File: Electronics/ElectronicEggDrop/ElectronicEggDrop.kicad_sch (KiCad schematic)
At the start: 10 parts, among them U1 LIS3DH

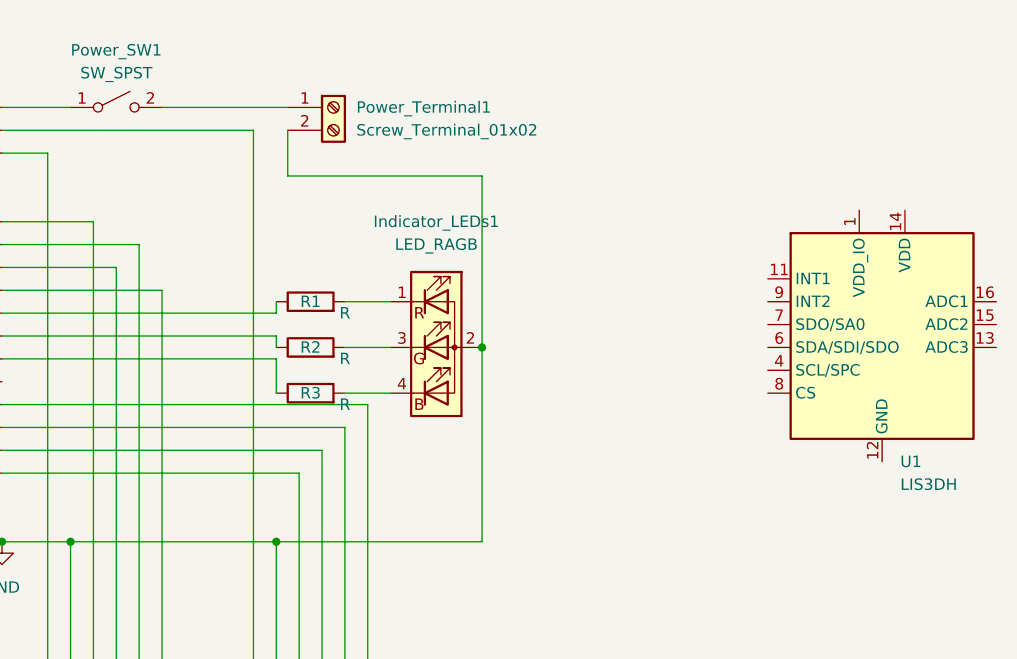
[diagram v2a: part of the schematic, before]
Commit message: Finished V1 of the Control and Sensor Egg boards, 3D models created by FreeCAD.  Need to fix code, assemble boards in FreeCAD, and create 3D printed housing
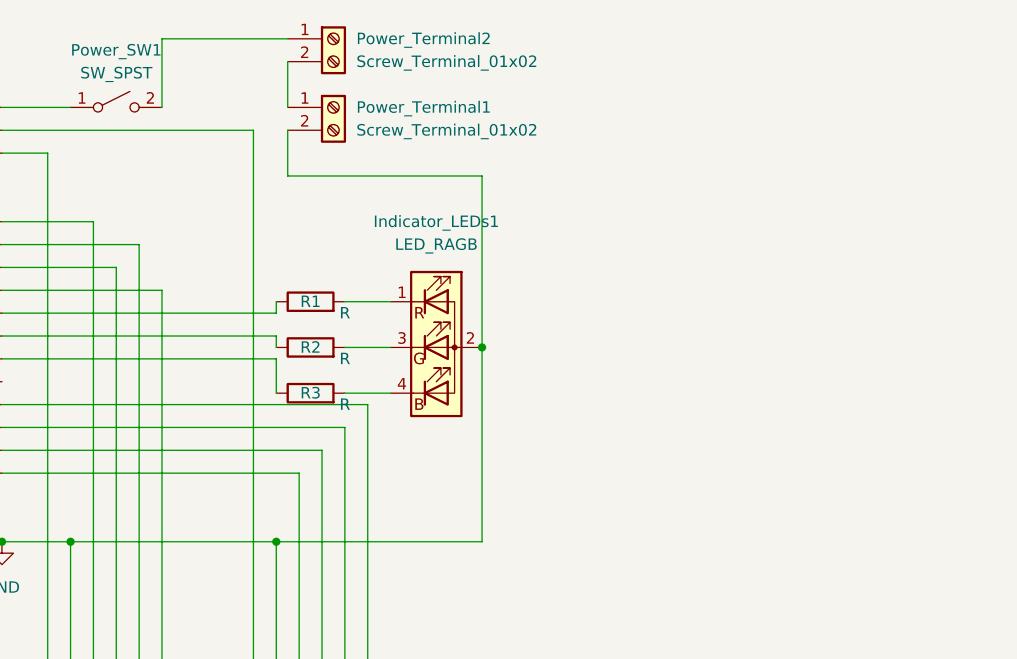
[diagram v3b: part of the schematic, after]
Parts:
- removed U1: LIS3DH, Package_LGA:LGA-16_3x3mm_P0.5mm_LayoutBorder3x5y, symbol Sensor_Motion:LIS3DH
- added Power_Terminal2: Screw_Terminal_01x02, Connector_JST:JST_PH_S2B-PH-K_1x02_P2.00mm_Horizontal, symbol Connector:Screw_Terminal_01x02
- Arduino_Nano1: footprint MODULE_ABX00053 -> Arduino Nano:MODULE_ABX00053
- Indicator_LEDs1: footprint Connector_Molex:Molex_KK-254_AE-6410-04A_1x04_P2.54mm_Vertical -> Connector_PinSocket_2.54mm:PinSocket_2x03_P2.54mm_Vertical
- LIS3DH_Connector1, SD_Card_Reader_Connector1: footprint Connector_Molex:Molex_KK-254_AE-6410-06A_1x06_P2.54mm_Vertical -> Connector_PinSocket_2.54mm:PinSocket_1x06_P2.54mm_Vertical
- Power_Terminal1: footprint TerminalBlock_Phoenix:TerminalBlock_Phoenix_MPT-0,5-2-2.54_1x02_P2.54mm_Horizontal -> Connector_JST:JST_PH_S2B-PH-K_1x02_P2.00mm_Horizontal
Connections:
- net at Power_SW1.2 (B): now also Power_Terminal2.1 (Pin_1); no longer Power_Terminal1.1 (Pin_1)
- new net: Power_Terminal1.1 (Pin_1), Power_Terminal2.2 (Pin_2)
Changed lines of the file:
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@@
   (junction (at 167.64 125.73) (diameter 0) (color 0 0 0 0)
   )
-  (wire (pts (xy 154.94 77.47) (xy 168.91 77.47))
-    (stroke (width 0) (type default) (color 0 0 0 0))
-  )
   (wire (pts (xy 147.32 144.78) (xy 147.32 90.17))
     (stroke (width 0) (type default) (color 0 0 0 0))
@@
     (stroke (width 0) (type default) (color 0 0 0 0))
   )
+  (wire (pts (xy 154.94 77.47) (xy 154.94 69.85))
+    (stroke (width 0) (type default) (color 0 0 0 0))
+  )
   (wire (pts (xy 190.5 104.14) (xy 190.5 125.73))
     (stroke (width 0) (type default) (color 0 0 0 0))
@@
     (stroke (width 0) (type default) (color 0 0 0 0))
   )
+  (wire (pts (xy 154.94 69.85) (xy 168.91 69.85))
+    (stroke (width 0) (type default) (color 0 0 0 0))
+  )
   (wire (pts (xy 165.1 80.01) (xy 137.16 80.01))
     (stroke (width 0) (type default) (color 0 0 0 0))
   )
   (wire (pts (xy 175.26 99.06) (xy 180.34 99.06))
+    (stroke (width 0) (type default) (color 0 0 0 0))
+  )
+  (wire (pts (xy 168.91 72.39) (xy 168.91 77.47))
     (stroke (width 0) (type default) (color 0 0 0 0))
   )
@@
     (property "Reference" "LIS3DH_Connector1" (id 0) (at 148.59 152.4 90))
     (property "Value" "Conn_01x06_Male" (id 1) (at 148.59 154.94 90))
-    (property "Footprint" "Connector_Molex:Molex_KK-254_AE-6410-06A_1x06_P2.54mm_Vertical" (id 2) (at 147.32 149.86 0)
+    (property "Footprint" "Connector_PinSocket_2.54mm:PinSocket_1x06_P2.54mm_Vertical" (id 2) (at 147.32 149.86 0)
       (effects (font (size 1.27 1.27)) hide)
     )
@@
     (pin "2")
   )
+  (symbol (lib_id "Connector:Screw_Terminal_01x02") (at 173.99 69.85 0) (unit 1)
+    (in_bom yes) (on_board yes) (fields_autoplaced)
+    (property "Reference" "Power_Terminal2" (id 0) (at 176.53 69.8499 0)
+      (effects (font (size 1.27 1.27)) (justify left))
+    )
+    (property "Value" "Screw_Terminal_01x02" (id 1) (at 176.53 72.3899 0)
+      (effects (font (size 1.27 1.27)) (justify left))
+    )
+    (property "Footprint" "Connector_JST:JST_PH_S2B-PH-K_1x02_P2.00mm_Horizontal" (id 2) (at 173.99 69.85 0)
+      (effects (font (size 1.27 1.27)) hide)
+    )
+    (property "Datasheet" "~" (id 3) (at 173.99 69.85 0)
+      (effects (font (size 1.27 1.27)) hide)
+    )
+    (pin "1")
+    (pin "2")
+  )
   (symbol (lib_id "power:GND") (at 137.16 125.73 0) (unit 1)
     (in_bom yes) (on_board yes) (fields_autoplaced)
@@
       (effects (font (size 1.27 1.27)) (justify left))
     )
-    (property "Footprint" "TerminalBlock_Phoenix:TerminalBlock_Phoenix_MPT-0,5-2-2.54_1x02_P2.54mm_Horizontal" (id 2) (at 173.99 77.47 0)
+    (property "Footprint" "Connector_JST:JST_PH_S2B-PH-K_1x02_P2.00mm_Horizontal" (id 2) (at 173.99 77.47 0)
       (effects (font (size 1.27 1.27)) hide)
     )
@@
     (property "Reference" "SD_Card_Reader_Connector1" (id 0) (at 171.45 152.4 90))
     (property "Value" "Conn_01x06_Male" (id 1) (at 171.45 154.94 90))
-    (property "Footprint" "Connector_Molex:Molex_KK-254_AE-6410-06A_1x06_P2.54mm_Vertical" (id 2) (at 170.18 149.86 0)
+    (property "Footprint" "Connector_PinSocket_2.54mm:PinSocket_1x06_P2.54mm_Vertical" (id 2) (at 170.18 149.86 0)
       (effects (font (size 1.27 1.27)) hide)
     )
@@
     (pin "6")
   )
-  (symbol (lib_id "Sensor_Motion:LIS3DH") (at 234.95 101.6 0) (unit 1)
-    (in_bom yes) (on_board yes) (fields_autoplaced)
-    (property "Reference" "U1" (id 0) (at 236.9694 116.84 0)
-      (effects (font (size 1.27 1.27)) (justify left))
-    )
-    (property "Value" "LIS3DH" (id 1) (at 236.9694 119.38 0)
-      (effects (font (size 1.27 1.27)) (justify left))
-    )
-    (property "Footprint" "Package_LGA:LGA-16_3x3mm_P0.5mm_LayoutBorder3x5y" (id 2) (at 237.49 128.27 0)
-      (effects (font (size 1.27 1.27)) hide)
-    )
-    (property "Datasheet" "https://www.st.com/resource/en/datasheet/cd00274221.pdf" (id 3) (at 229.87 104.14 0)
-      (effects (font (size 1.27 1.27)) hide)
-    )
-    (pin "1")
-    (pin "10")
-    (pin "11")
-    (pin "12")
-    (pin "13")
-    (pin "14")
-    (pin "15")
-    (pin "16")
-    (pin "2")
-    (pin "3")
-    (pin "4")
-    (pin "5")
-    (pin "6")
-    (pin "7")
-    (pin "8")
-    (pin "9")
-  )
   (symbol (lib_id "ABX00053:ABX00053") (at 111.76 100.33 0) (unit 1)
     (in_bom yes) (on_board yes) (fields_autoplaced)
     (property "Reference" "Arduino_Nano1" (id 0) (at 111.76 69.85 0))
     (property "Value" "ABX00053" (id 1) (at 111.76 72.39 0))
-    (property "Footprint" "MODULE_ABX00053" (id 2) (at 111.76 100.33 0)
+    (property "Footprint" "Arduino Nano:MODULE_ABX00053" (id 2) (at 111.76 100.33 0)
       (effects (font (size 1.27 1.27)) (justify left bottom) hide)
     )
@@
     (property "Reference" "Indicator_LEDs1" (id 0) (at 185.42 90.17 0))
     (property "Value" "LED_RAGB" (id 1) (at 185.42 92.71 0))
-    (property "Footprint" "Connector_Molex:Molex_KK-254_AE-6410-04A_1x04_P2.54mm_Vertical" (id 2) (at 185.42 105.41 0)
+    (property "Footprint" "Connector_PinSocket_2.54mm:PinSocket_2x03_P2.54mm_Vertical" (id 2) (at 185.42 105.41 0)
       (effects (font (size 1.27 1.27)) hide)
     )
@@
     )
     (path "/e0dad96b-23b2-46bc-93d4-eedf18ddd013"
-      (reference "Arduino_Nano1") (unit 1) (value "ABX00053") (footprint "MODULE_ABX00053")
+      (reference "Arduino_Nano1") (unit 1) (value "ABX00053") (footprint "Arduino Nano:MODULE_ABX00053")
     )
     (path "/f7aa1d10-f8d1-4fe6-acb4-10abc2244f09"
-      (reference "Indicator_LEDs1") (unit 1) (value "LED_RAGB") (footprint "Connector_Molex:Molex_KK-254_AE-6410-04A_1x04_P2.54mm_Vertical")
+      (reference "Indicator_LEDs1") (unit 1) (value "LED_RAGB") (footprint "Connector_PinSocket_2.54mm:PinSocket_2x03_P2.54mm_Vertical")
     )
     (path "/432a2ef5-8c4c-4a55-bf4b-ba5b90ca0b70"
-      (reference "LIS3DH_Connector1") (unit 1) (value "Conn_01x06_Male") (footprint "Connector_Molex:Molex_KK-254_AE-6410-06A_1x06_P2.54mm_Vertical")
+      (reference "LIS3DH_Connector1") (unit 1) (value "Conn_01x06_Male") (footprint "Connector_PinSocket_2.54mm:PinSocket_1x06_P2.54mm_Vertical")
     )
     (path "/3bd3481f-6f6f-4cff-8d9c-7c9dc14e3fc3"
@@
     )
     (path "/c79642f2-5f2f-4055-93db-5cce65ec58b5"
-      (reference "Power_Terminal1") (unit 1) (value "Screw_Terminal_01x02") (footprint "TerminalBlock_Phoenix:TerminalBlock_Phoenix_MPT-0,5-2-2.54_1x02_P2.54mm_Horizontal")
+      (reference "Power_Terminal1") (unit 1) (value "Screw_Terminal_01x02") (footprint "Connector_JST:JST_PH_S2B-PH-K_1x02_P2.00mm_Horizontal")
+    )
+    (path "/aa73b884-c23f-4aa6-ae16-3e4265a1b7ca"
+      (reference "Power_Terminal2") (unit 1) (value "Screw_Terminal_01x02") (footprint "Connector_JST:JST_PH_S2B-PH-K_1x02_P2.00mm_Horizontal")
     )
     (path "/27354c14-7ea3-4310-8f3a-463ad49a3e7f"
@@
     )
     (path "/c93ef0e7-749a-4bd6-b03c-c57ac7336301"
-      (reference "SD_Card_Reader_Connector1") (unit 1) (value "Conn_01x06_Male") (footprint "Connector_Molex:Molex_KK-254_AE-6410-06A_1x06_P2.54mm_Vertical")
-    )
-    (path "/d52348c1-93f5-4f4d-9809-0125366275cf"
-      (reference "U1") (unit 1) (value "LIS3DH") (footprint "Package_LGA:LGA-16_3x3mm_P0.5mm_LayoutBorder3x5y")
-    )
-  )
+      (reference "SD_Card_Reader_Connector1") (unit 1) (value "Conn_01x06_Male") (footprint "Connector_PinSocket_2.54mm:PinSocket_1x06_P2.54mm_Vertical")
+    )
+  )

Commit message: Finished the PCBs
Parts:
- Power_SW1: footprint Connector_Molex:Molex_KK-254_AE-6410-02A_1x02_P2.54mm_Vertical -> Connector_PinSocket_2.54mm:PinSocket_1x02_P2.54mm_Vertical
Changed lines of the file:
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@@
     (property "Reference" "Power_SW1" (id 0) (at 149.86 71.12 0))
     (property "Value" "SW_SPST" (id 1) (at 149.86 73.66 0))
-    (property "Footprint" "Connector_Molex:Molex_KK-254_AE-6410-02A_1x02_P2.54mm_Vertical" (id 2) (at 149.86 77.47 0)
+    (property "Footprint" "Connector_PinSocket_2.54mm:PinSocket_1x02_P2.54mm_Vertical" (id 2) (at 149.86 77.47 0)
       (effects (font (size 1.27 1.27)) hide)
     )
@@
     )
     (path "/3bd3481f-6f6f-4cff-8d9c-7c9dc14e3fc3"
-      (reference "Power_SW1") (unit 1) (value "SW_SPST") (footprint "Connector_Molex:Molex_KK-254_AE-6410-02A_1x02_P2.54mm_Vertical")
+      (reference "Power_SW1") (unit 1) (value "SW_SPST") (footprint "Connector_PinSocket_2.54mm:PinSocket_1x02_P2.54mm_Vertical")
     )
     (path "/c79642f2-5f2f-4055-93db-5cce65ec58b5"
